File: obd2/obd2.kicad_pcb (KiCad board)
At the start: 2 copper layers, 80 x 49 mm, 59 parts, among them J1 RJ45_BASIC, J2 MICRO_SD, K1 UART, P1 JTAG_PROG, P2 IO_1, P3 IO_2, SW1 SW_OFF_MOM, SW2 SW_OFF_MOM, SW3 SW_OFF_MOM, SW4 PWR_SW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

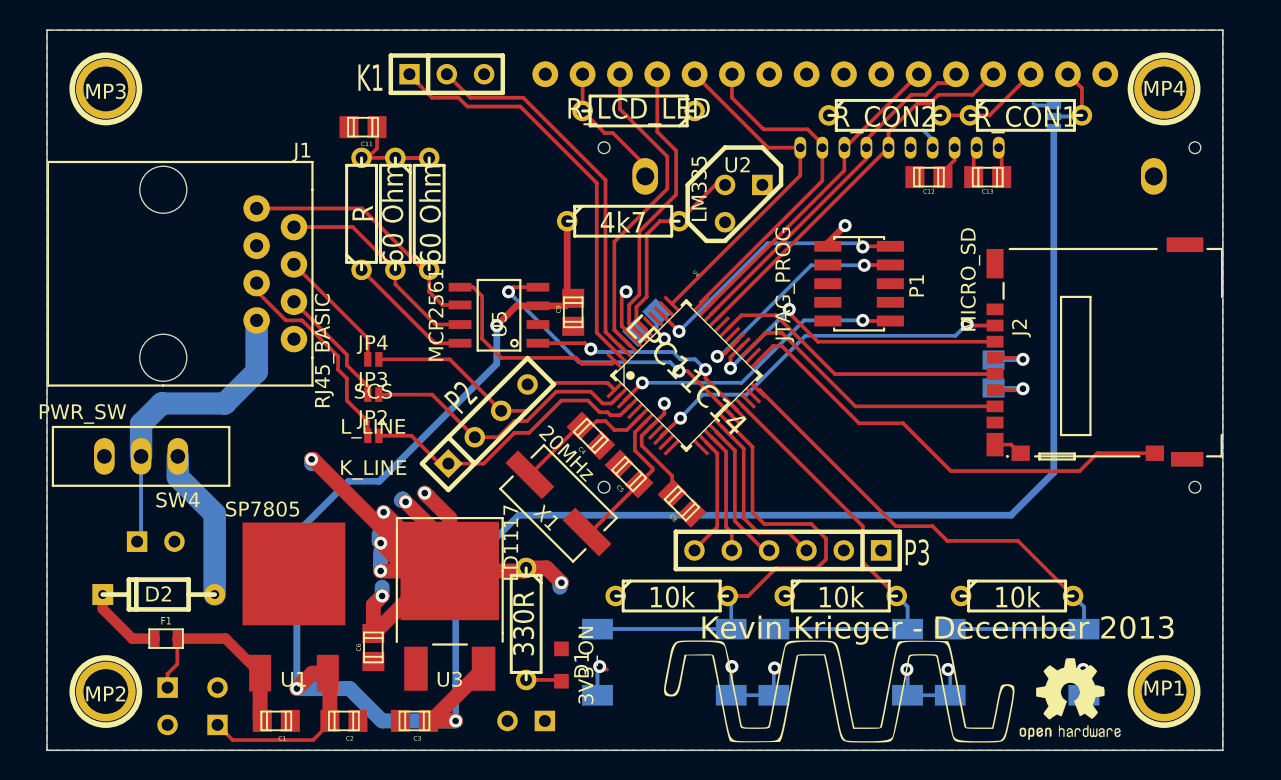
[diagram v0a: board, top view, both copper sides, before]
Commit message: Moved components to add enough room for 4-40 hardware. Moved all silkscreen values to appropriate places. rev 1 finished and ordered.
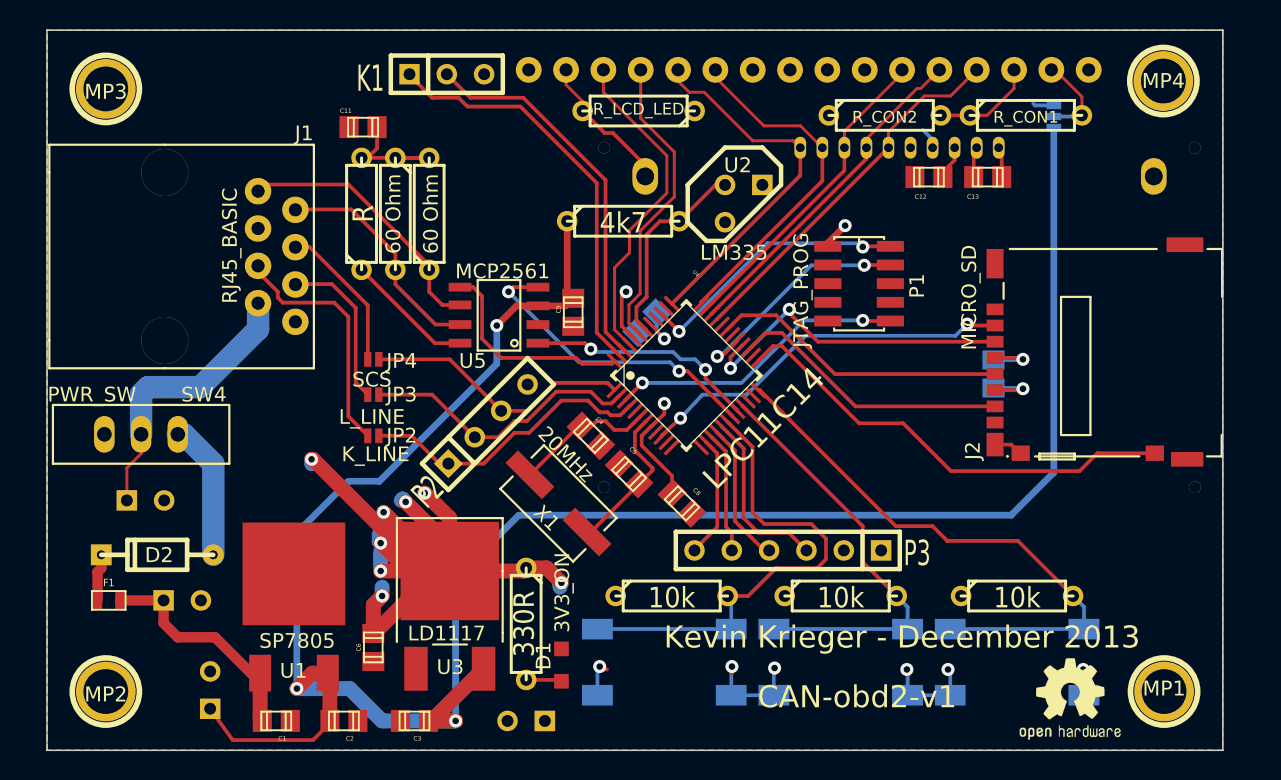
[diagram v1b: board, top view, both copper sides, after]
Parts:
- removed the G*** at (165.4, 134.5)
- moved W4 7.27 mm to (120.7, 128.3), turned to 0 degrees
- moved F1 4.69 mm to (115.7, 128.3)
- moved W1 2.89 mm to (118.2, 121.5)
- moved D2 2.70 mm to (119.0, 125.2)
- moved SW4 1.50 mm to (117.9, 117.0)
- moved W2 1.21 mm to (122.6, 134.4)
- moved J1 1.18 mm to (128.4, 101.7)
- moved LCD1 1.17 mm to (182.4, 92.2)
- moved MP4 0.54 mm to (187.5, 93.0)
- renumbered SW3 to 1, SW2 to 2, SW1 to 3
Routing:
- net L_LINE: track 8.40 -> 11.0 mm
- net K_LINE: track 14.2 -> 16.7 mm
- net +12V: track 13.5 -> 15.8 mm
- net N-0000073: track 5.37 -> 3.20 mm
- net SCS: track 8.54 -> 10.3 mm
- net VBAT: track 20.9 -> 19.2 mm
- net LCD_DB5/RST: track 23.5 -> 25.2 mm
- net +5V: track 153.1 -> 154.3 mm
- net CAN_L: track 14.6 -> 15.7 mm
- net N-0000026: track 10.4 -> 9.44 mm
- net LCD_RS/SI: track 26.4 -> 25.4 mm
- net LCD_RW/RS: track 24.2 -> 23.2 mm
- net CAN_H: track 17.4 -> 18.4 mm
- net N-0000049: track 5.16 -> 6.07 mm
- net N-0000050: track 9.04 -> 9.81 mm
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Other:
- board text added: "CAN-obd2-v1"
